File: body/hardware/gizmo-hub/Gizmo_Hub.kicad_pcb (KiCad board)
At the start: 2 copper layers, 75 x 70 mm, 23 parts, among them J1 DISPLAY, J10 FUTURE, J2 SPEAKER 3885, J3 BUTTONS, J4 PTT, J5 HAPTIC, J6 PWR, J7 UTIL, J8 5V AUX A, J9 5V AUX B, U1 XIAO ESP32S3 Sense

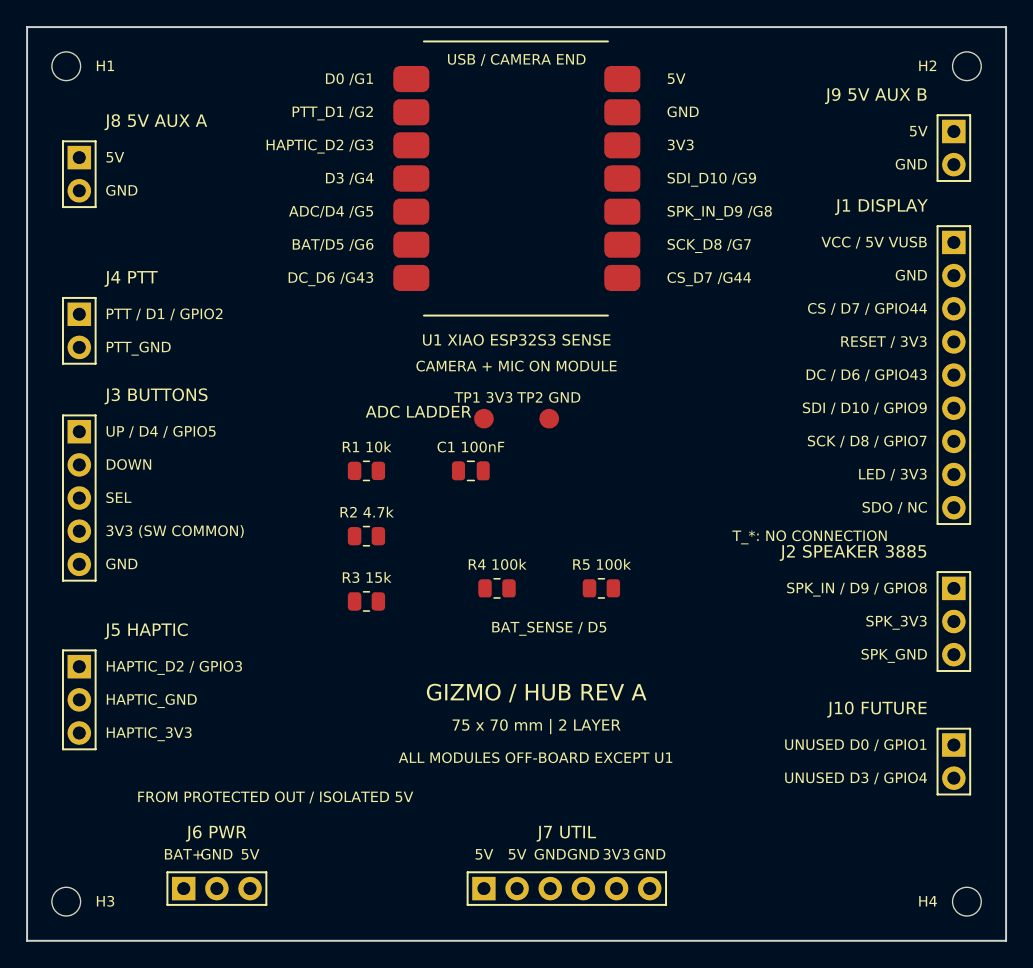
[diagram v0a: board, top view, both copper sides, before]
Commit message: Complete Gizmo hub routing, battery clearance, and wiring documentation
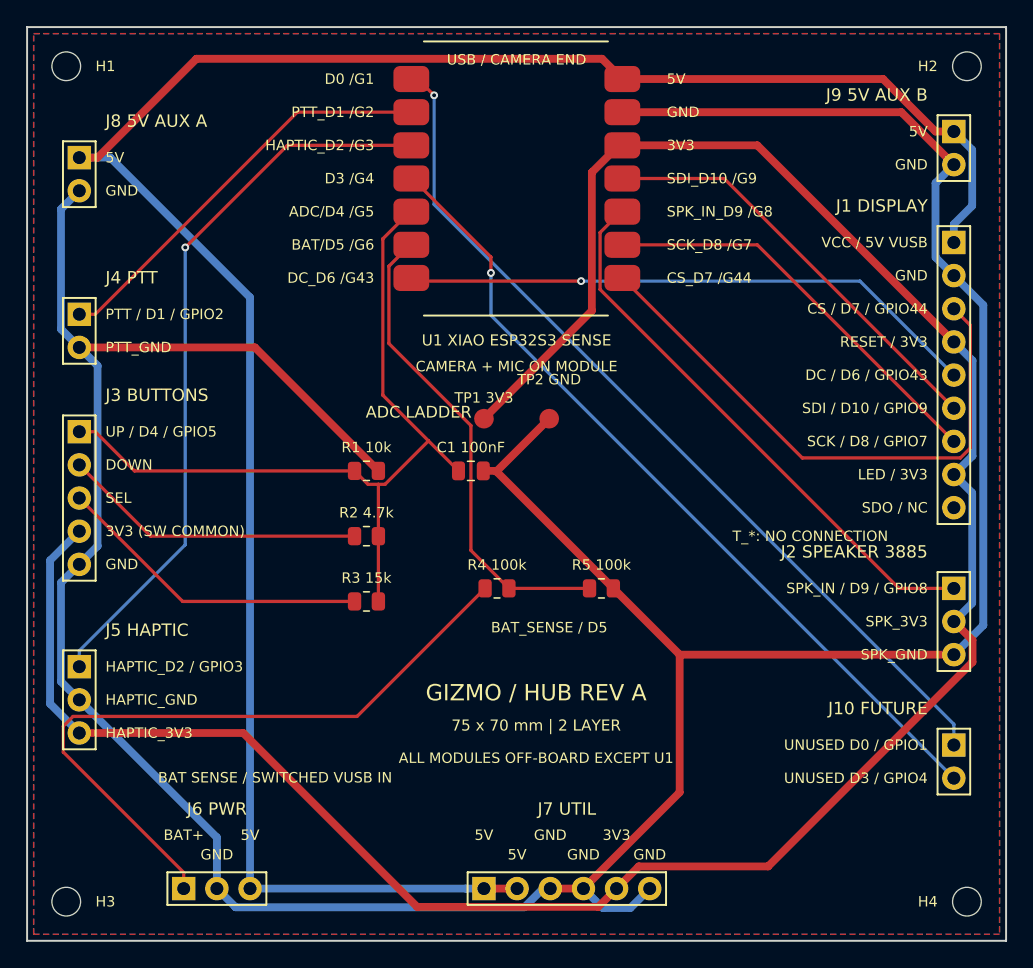
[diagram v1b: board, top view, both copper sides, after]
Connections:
- net 3V3 renamed /3V3
- net 5V renamed /5V
- net BAT+ renamed /BAT+
- net BAT_SENSE_D5_GPIO6 renamed /BAT_SENSE_D5_GPIO6
- net BUTTON_ADC_D4_GPIO5 renamed /BUTTON_ADC_D4_GPIO5
- net BUTTON_DOWN renamed /BUTTON_DOWN
- net BUTTON_SEL renamed /BUTTON_SEL
- net D0_GPIO1_UNUSED renamed /D0_GPIO1_UNUSED
- net D3_GPIO4_UNUSED renamed /D3_GPIO4_UNUSED
- net DISP_CS_D7_GPIO44 renamed /DISP_CS_D7_GPIO44
- net DISP_DC_D6_GPIO43 renamed /DISP_DC_D6_GPIO43
- net DISP_SCK_D8_GPIO7 renamed /DISP_SCK_D8_GPIO7
- net DISP_SDI_D10_GPIO9 renamed /DISP_SDI_D10_GPIO9
- net GND renamed /GND
- net HAPTIC_D2_GPIO3 renamed /HAPTIC_D2_GPIO3
- net PTT_D1_GPIO2 renamed /PTT_D1_GPIO2
- net SPK_IN_D9_GPIO8 renamed /SPK_IN_D9_GPIO8
- J1 pad 9: (no net) -> unconnected-(J1-SDO_/_NC-Pad9)
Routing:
- net /GND: track 0.00 -> 259.9 mm
- net /3V3: track 0.00 -> 183.6 mm
- net /5V: track 0.00 -> 165.4 mm
- net /D0_GPIO1_UNUSED: track 0.00 -> 68.5 mm, vias 0 -> 1
- net /D3_GPIO4_UNUSED: track 0.00 -> 63.2 mm, vias 0 -> 1
- net /BUTTON_ADC_D4_GPIO5: track 0.00 -> 62.0 mm
- net /HAPTIC_D2_GPIO3: track 0.00 -> 56.0 mm, vias 0 -> 1
- net /BAT+: track 0.00 -> 53.0 mm
- net /DISP_DC_D6_GPIO43: track 0.00 -> 44.6 mm, vias 0 -> 1
- net /DISP_CS_D7_GPIO44: track 0.00 -> 43.9 mm
- net /SPK_IN_D9_GPIO8: track 0.00 -> 43.3 mm
- net /BAT_SENSE_D5_GPIO6: track 0.00 -> 37.1 mm
- net /DISP_SDI_D10_GPIO9: track 0.00 -> 32.7 mm
- net /PTT_D1_GPIO2: track 0.00 -> 31.8 mm
- net /DISP_SCK_D8_GPIO7: track 0.00 -> 31.6 mm
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- added copper zone on B.Cu, net /GND
- added copper zone on F.Cu, net /GND
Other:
- board text added: "BAT SENSE / SWITCHED VUSB IN"
- board text removed: "FROM PROTECTED OUT / ISOLATED 5V"
